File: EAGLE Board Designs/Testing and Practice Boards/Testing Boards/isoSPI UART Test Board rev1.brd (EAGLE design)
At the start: 160 x 100 mm, 51 parts, among them J1 CONNECTOR-6_μF_T_V_BLACK, J2 CONNECTOR-2_MF_T_V_, J4 CONNECTOR-2_MF_T_V_, J5 CONNECTOR-6_μF_T_V_BLACK, T1 78613/3C, T2 78613/3C, U1 MCP3204, U2 ADM4854ARZ, U3 LTC6820, U4 OPAMP_1_CHANNEL_OPA991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

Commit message: brd rev1 ready for review
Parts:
- added U$1, U$2, U$3, U$4: (no value), HyTechManufacturing:MOUNTING_M3
- added U$5: (no value), HyTechManufacturing:LOGO_HYTECH_MEDIUM
- added U$6: (no value), HyTechManufacturing:LOGO_GT_MEDIUM
- moved R20 24.5 mm to (48.5, 47.8), turned to 180 degrees
- moved R19 21.2 mm to (49.8, 49.5), turned to 180 degrees
- moved C1 17.7 mm to (57.4, 48.8)
- moved C2 17.7 mm to (57.4, 47.2)
- moved R18 17.5 mm to (49.5, 43.9), turned to 270 degrees
- moved U3 15.5 mm to (53.6, 46.7), turned to 0 degrees
- moved TP1 14.4 mm to (88.4, 20.8)
- moved R26 13.3 mm to (51.8, 41.4), turned to 270 degrees
- moved C3 12.6 mm to (32.0, 11.9), turned to 180 degrees
- moved R25 11.2 mm to (36.8, 45.7)
- moved R24 10.9 mm to (36.6, 31.5)
- moved C4 10.2 mm to (32.0, 13.7), turned to 180 degrees
- moved J2 8.89 mm to (13.0, 45.7)
- moved J4 8.89 mm to (13.0, 31.5)
- moved T2 8.89 mm to (26.2, 45.7)
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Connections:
- net IP_1 renamed DIFF_1_P
- net IP_2 renamed DIFF_2_P
- net TX+ renamed TX_P
- net TX- renamed TX_N
- removed net IM_1: R24.1, T1.2, U3.10
- removed net IM_2: R25.1, T2.2, U7.10
- removed net RX+: C7.2, D2.1, J5.2, U2.8
- removed net RX-: D2.2, J5.3, R7.1, U2.7
- new net DIFF_1_N: R24.1, T1.3, U3.10
- new net DIFF_2_N: R25.1, T2.3, U7.10
- new net RX_N: D2.1, J5.3, R7.1, U2.7
- new net RX_P: C7.2, D2.2, J5.2, U2.8
- net N$18: now also T1.2; no longer T1.3
- net N$19: now also T2.2; no longer T2.3
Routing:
- net +3V3: track 42.7 -> 192.9 mm
- net DIFF_2_P: track 0.00 -> 59.5 mm
- net DIFF_2_N: track 0.00 -> 59.5 mm
- net GND: track 0.00 -> 47.6 mm, vias 0 -> 24
- net RX_P: track 0.00 -> 44.9 mm
- net RX_N: track 0.00 -> 44.1 mm
- net DIFF_1_N: track 0.00 -> 42.1 mm
- net DIFF_1_P: track 0.00 -> 41.2 mm
- net TX_N: track 0.00 -> 33.6 mm
- net TX_P: track 0.00 -> 31.7 mm
- net UART_RX: track 5.03 -> 18.3 mm
- net UART_TX: track 5.03 -> 17.8 mm
- net TEENSY_CLK: track 23.0 -> 11.5 mm
- net TEENSY_CS: track 7.08 -> 18.0 mm
- net ADC_SDO: track 0.00 -> 10.8 mm
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- added copper zone on layer 16, net GND
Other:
- board size 160 x 100 mm -> 101.6 x 61 mm
- board text added: "HyTech Racing 2024 isoSPI UART Test Board rev1 Designed by Eric Galluzzi"

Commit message: woo
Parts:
- moved R6 0.80 mm to (78.5, 20.6)
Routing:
- net N$8: track 3.50 -> 2.63 mm
- net +3V3: track 192.9 -> 192.1 mm
- net N$9: track 3.29 -> 2.63 mm
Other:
- outline, holes or cut-outs redrawn
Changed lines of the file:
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@@
 <board>
 <plain>
-<wire x1="0" y1="58.42" x2="0" y2="2.54" width="0" layer="20"/>
+<wire x1="99.06" y1="60.96" x2="5" y2="60.96" width="0" layer="20"/>
+<wire x1="5" y1="60.96" x2="0" y2="55.96" width="0" layer="20" curve="90"/>
+<wire x1="0" y1="55.96" x2="0" y2="2.54" width="0" layer="20"/>
 <wire x1="0" y1="2.54" x2="2.54" y2="0" width="0" layer="20" curve="90"/>
 <wire x1="2.54" y1="0" x2="99.06" y2="0" width="0" layer="20"/>
@@
 <wire x1="101.6" y1="2.54" x2="101.6" y2="58.42" width="0" layer="20"/>
 <wire x1="101.6" y1="58.42" x2="99.06" y2="60.96" width="0" layer="20" curve="90"/>
-<wire x1="99.06" y1="60.96" x2="2.54" y2="60.96" width="0" layer="20"/>
-<wire x1="2.54" y1="60.96" x2="0" y2="58.42" width="0" layer="20" curve="90"/>
 <text x="46.228" y="55.88" size="0.8128" layer="25" font="vector">HyTech Racing 2024
 isoSPI UART Test Board rev1
@@
 <attribute name="VOLTAGE_MAX" value="75V" x="30.48" y="96.266" size="1.778" layer="27" rot="R180" display="off"/>
 </element>
-<element name="R6" library="HyTechDevices" package="0603-RES" value="RESISTOR_0603_2.74K" x="77.724" y="20.828" smashed="yes" rot="R270">
-<attribute name="DKPN" value="P20020CT-ND" x="7.874" y="-36.322" size="1.778" layer="27" rot="R270" display="off"/>
-<attribute name="MANUFACTURER" value="Panasonic Electronic Components" x="7.874" y="-36.322" size="1.778" layer="27" rot="R270" display="off"/>
-<attribute name="MOPN" value="667-ERJ-PB3B2741V" x="7.874" y="-36.322" size="1.778" layer="27" rot="R270" display="off"/>
-<attribute name="MPN" value="ERJ-PB3B2741V" x="7.874" y="-36.322" size="1.778" layer="27" rot="R270" display="off"/>
-<attribute name="NAME" x="76.073" y="20.828" size="0.8128" layer="25" font="vector" rot="R270" align="bottom-center"/>
-<attribute name="POWER" value="0.2W" x="7.874" y="-36.322" size="1.778" layer="27" rot="R270" display="off"/>
-<attribute name="RESISTANCE" value="2.74k" x="7.874" y="-36.322" size="1.778" layer="27" rot="R270" display="off"/>
-<attribute name="TOLERANCE" value="0.1%" x="7.874" y="-36.322" size="1.778" layer="27" rot="R270" display="off"/>
-<attribute name="VOLTAGE_CONTINUOUS" value="23.41V" x="7.874" y="-36.322" size="1.778" layer="27" rot="R270" display="off"/>
-<attribute name="VOLTAGE_MAX" value="150V" x="7.874" y="-36.322" size="1.778" layer="27" rot="R270" display="off"/>
+<element name="R6" library="HyTechDevices" package="0603-RES" value="RESISTOR_0603_2.74K" x="78.486" y="20.574" smashed="yes" rot="R270">
+<attribute name="DKPN" value="P20020CT-ND" x="8.636" y="-36.576" size="1.778" layer="27" rot="R270" display="off"/>
+<attribute name="MANUFACTURER" value="Panasonic Electronic Components" x="8.636" y="-36.576" size="1.778" layer="27" rot="R270" display="off"/>
+<attribute name="MOPN" value="667-ERJ-PB3B2741V" x="8.636" y="-36.576" size="1.778" layer="27" rot="R270" display="off"/>
+<attribute name="MPN" value="ERJ-PB3B2741V" x="8.636" y="-36.576" size="1.778" layer="27" rot="R270" display="off"/>
+<attribute name="NAME" x="76.835" y="20.574" size="0.8128" layer="25" font="vector" rot="R270" align="bottom-center"/>
+<attribute name="POWER" value="0.2W" x="8.636" y="-36.576" size="1.778" layer="27" rot="R270" display="off"/>
+<attribute name="RESISTANCE" value="2.74k" x="8.636" y="-36.576" size="1.778" layer="27" rot="R270" display="off"/>
+<attribute name="TOLERANCE" value="0.1%" x="8.636" y="-36.576" size="1.778" layer="27" rot="R270" display="off"/>
+<attribute name="VOLTAGE_CONTINUOUS" value="23.41V" x="8.636" y="-36.576" size="1.778" layer="27" rot="R270" display="off"/>
+<attribute name="VOLTAGE_MAX" value="150V" x="8.636" y="-36.576" size="1.778" layer="27" rot="R270" display="off"/>
 </element>
 <element name="R7" library="HyTechDevices" package="0603-RES" value="RESISTOR_0603_DNP" x="28.194" y="19.304" smashed="yes" rot="R90">
@@
 <attribute name="MOPN" value="595-INA823DT" x="131.826" y="-36.576" size="1.778" layer="27" display="off"/>
 <attribute name="MPN" value="INA823DT" x="131.826" y="-36.576" size="1.778" layer="27" display="off"/>
-<attribute name="NAME" x="79.375" y="21.59" size="0.8128" layer="25" font="vector" rot="R90" align="bottom-center"/>
+<attribute name="NAME" x="85.979" y="20.32" size="0.8128" layer="25" font="vector" rot="R90" align="bottom-center"/>
 </element>
 <element name="U7" library="HyTechDevices" package="MSOP-16" value="LTC6820" x="83.82" y="43.688" smashed="yes" rot="R90">
@@
 <wire x1="59.194" y1="51.308" x2="56.654" y2="48.768" width="0.254" layer="1"/>
 <wire x1="51.474" y1="40.552" x2="50.292" y2="39.37" width="0.254" layer="1"/>
-<wire x1="50.292" y1="39.37" x2="49.276" y2="38.354" width="0.254" layer="1"/>
 <wire x1="51.474" y1="40.552" x2="51.816" y2="40.552" width="0.254" layer="1"/>
 <wire x1="49.53" y1="40.132" x2="50.292" y2="39.37" width="0.254" layer="1"/>
 <wire x1="49.53" y1="40.132" x2="49.53" y2="43.092" width="0.254" layer="1"/>
-<wire x1="49.276" y1="23.622" x2="52.832" y2="20.066" width="0.254" layer="1"/>
-<wire x1="49.276" y1="38.354" x2="49.276" y2="23.622" width="0.254" layer="1"/>
+<wire x1="50.292" y1="22.606" x2="52.832" y2="20.066" width="0.254" layer="1"/>
+<wire x1="50.292" y1="39.37" x2="50.292" y2="22.606" width="0.254" layer="1"/>
 <wire x1="70.358" y1="28.956" x2="65.786" y2="28.956" width="0.254" layer="1"/>
 <wire x1="65.786" y1="28.956" x2="64.008" y2="27.178" width="0.254" layer="1"/>
@@
 <wire x1="36.957" y1="21.717" x2="36.957" y2="20.6375" width="0.254" layer="1"/>
 <wire x1="36.576" y1="22.098" x2="36.957" y2="21.717" width="0.254" layer="1"/>
-<wire x1="24.9776625" y1="15.1384" x2="27.8384" y2="15.1384" width="0.254" layer="1"/>
+<wire x1="24.9776625" y1="15.1384" x2="25.908" y2="15.1384" width="0.254" layer="1"/>
+<wire x1="25.908" y1="15.1384" x2="27.8384" y2="15.1384" width="0.254" layer="1"/>
 <wire x1="27.8384" y1="15.1384" x2="29.8704" y2="17.1704" width="0.254" layer="1"/>
 <wire x1="29.8704" y1="17.1704" x2="35.2044" y2="17.1704" width="0.254" layer="1"/>
@@
 <wire x1="87.718" y1="30.48" x2="89.408" y2="28.79" width="0.254" layer="1"/>
 <wire x1="89.408" y1="28.79" x2="89.408" y2="28.182" width="0.254" layer="1"/>
-<wire x1="84.216" y1="30.564" x2="85.402" y2="31.75" width="0.254" layer="1"/>
-<wire x1="86.448" y1="31.75" x2="87.718" y2="30.48" width="0.254" layer="1"/>
-<wire x1="85.402" y1="31.75" x2="86.448" y2="31.75" width="0.254" layer="1"/>
+<wire x1="84.216" y1="30.564" x2="85.148" y2="31.496" width="0.254" layer="1"/>
+<wire x1="86.702" y1="31.496" x2="87.718" y2="30.48" width="0.254" layer="1"/>
+<wire x1="85.148" y1="31.496" x2="86.702" y2="31.496" width="0.254" layer="1"/>
 <wire x1="84.216" y1="30.564" x2="83.284" y2="31.496" width="0.254" layer="1"/>
 <wire x1="83.284" y1="31.496" x2="81.788" y2="31.496" width="0.254" layer="1"/>
@@
 <contactref element="U5" pad="1"/>
 <contactref element="R6" pad="2"/>
-<wire x1="77.724" y1="19.978" x2="79.7315" y2="17.9705" width="0.254" layer="1"/>
-<wire x1="79.7315" y1="17.9705" x2="80.391" y2="17.9705" width="0.254" layer="1"/>
+<wire x1="78.486" y1="19.724" x2="80.2395" y2="17.9705" width="0.254" layer="1"/>
+<wire x1="80.2395" y1="17.9705" x2="80.391" y2="17.9705" width="0.254" layer="1"/>
 </signal>
 <signal name="N$9" airwireshidden="yes">
 <contactref element="R6" pad="1"/>
 <contactref element="U5" pad="8"/>
-<wire x1="77.724" y1="21.678" x2="79.2235" y2="23.1775" width="0.254" layer="1"/>
-<wire x1="79.2235" y1="23.1775" x2="80.391" y2="23.1775" width="0.254" layer="1"/>
+<wire x1="78.486" y1="21.424" x2="80.2395" y2="23.1775" width="0.254" layer="1"/>
+<wire x1="80.2395" y1="23.1775" x2="80.391" y2="23.1775" width="0.254" layer="1"/>
 </signal>
 <signal name="CH_1-" airwireshidden="yes">

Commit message: board review
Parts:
- moved J1 1.78 mm to (84.8, 8.64), flipped to the top, turned to 270 degrees
- moved U$5 1.02 mm to (10.2, 53.3)
- moved C20 0.76 mm to (34.0, 46.5)
- moved J2 0.76 mm to (13.0, 46.5)
- moved R25 0.76 mm to (36.8, 46.5)
- moved T2 0.76 mm to (26.2, 46.5)
- moved D2 0.36 mm to (20.8, 19.6)
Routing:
- net CH3: track 39.5 -> 48.4 mm
- net CH2: track 33.8 -> 39.8 mm
- net TX_P: track 31.7 -> 37.6 mm
- net TX_N: track 33.6 -> 39.5 mm
- net CH_1+: track 5.35 -> 10.1 mm
- net 5VIN: track 12.5 -> 9.67 mm
- net DIFF_1_N: track 42.1 -> 39.3 mm
- net CH_1-: track 4.63 -> 6.41 mm
- net DIFF_2_N: track 59.5 -> 57.9 mm
- net +3V3: track 192.1 -> 193.4 mm
- net DIFF_2_P: track 59.5 -> 58.2 mm
- net DIFF_1_P: track 41.2 -> 40.1 mm
- net UART_RX: track 18.3 -> 19.0 mm
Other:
- outline, holes or cut-outs redrawn

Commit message: awesome
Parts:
- added R2: RESISTOR_1206_HV46.4K, HyTechDevices:1206-RES
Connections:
- net +3V3: now also R2.1
- net GND: now also R2.2
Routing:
- net +3V3: track 193.4 -> 201.1 mm
- net N$7: track 0.00 -> 1.88 mm, vias 0 -> 1

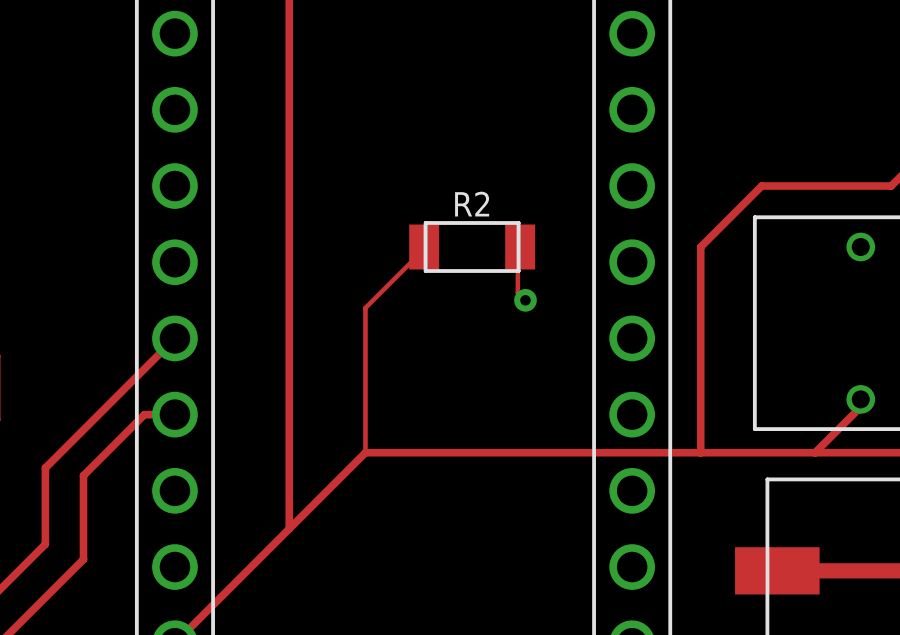
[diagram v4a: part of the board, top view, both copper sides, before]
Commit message: There was a resistor added!
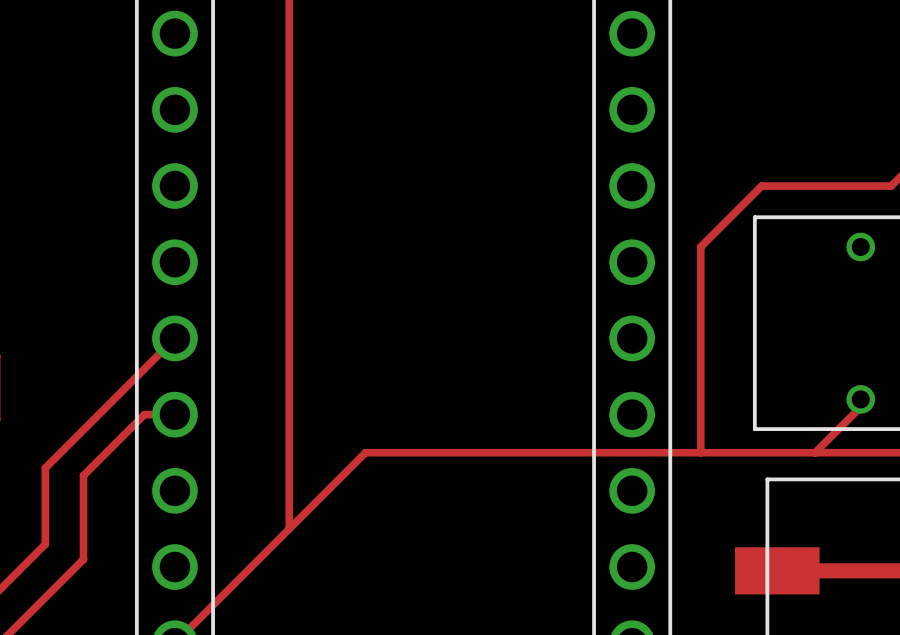
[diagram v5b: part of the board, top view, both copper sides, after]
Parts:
- removed R2: RESISTOR_1206_HV46.4K, HyTechDevices:1206-RES
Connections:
- net +3V3: no longer R2.1
- net GND: no longer R2.2
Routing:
- net +3V3: track 201.1 -> 193.4 mm
- net N$7: track 1.88 -> 0.00 mm, vias 1 -> 0
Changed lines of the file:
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@@
 <attribute name="NAME" x="19.05" y="18.542" size="0.635" layer="25" font="vector" rot="R270" align="top-center"/>
-</element>
-<element name="R2" library="HyTechDevices" package="1206-RES" value="RESISTOR_1206_HV46.4K" x="56.388" y="26.924" smashed="yes">
-<attribute name="DKPN" value="RHM46.4KAICT-ND" x="56.388" y="26.924" size="1.778" layer="27" display="off"/>
-<attribute name="MANUFACTURER" value="Rohm Semiconductor" x="56.388" y="26.924" size="1.778" layer="27" display="off"/>
-<attribute name="MOPN" value="755-KTR18EZPF4642" x="56.388" y="26.924" size="1.778" layer="27" display="off"/>
-<attribute name="MPN" value="KTR18EZPF4642" x="56.388" y="26.924" size="1.778" layer="27" display="off"/>
-<attribute name="NAME" x="56.388" y="27.94" size="0.8128" layer="25" font="vector" align="bottom-center"/>
-<attribute name="POWER" value="0.25W" x="56.388" y="26.924" size="1.778" layer="27" display="off"/>
-<attribute name="RESISTANCE" value="46.4k" x="56.388" y="26.924" size="1.778" layer="27" display="off"/>
-<attribute name="TOLERANCE" value="1%" x="56.388" y="26.924" size="1.778" layer="27" display="off"/>
-<attribute name="VOLTAGE_CONTINUOUS" value="107.7V" x="56.388" y="26.924" size="1.778" layer="27" display="off"/>
-<attribute name="VOLTAGE_MAX" value="500V" x="56.388" y="26.924" size="1.778" layer="27" display="off"/>
 </element>
 </elements>
@@
 <wire x1="19.8247" y1="19.558" x2="18.542" y2="19.558" width="0.254" layer="1"/>
 <via x="18.542" y="19.558" extent="1-16" drill="0.3556"/>
-<contactref element="R2" pad="2"/>
 <wire x1="85.9255" y1="44.938" x2="88.888" y2="44.958" width="0" layer="19" extent="1-1"/>
 <wire x1="85.9255" y1="41.938" x2="85.9255" y2="44.938" width="0" layer="19" extent="1-1"/>
@@
 <wire x1="16.002" y1="17.7292" x2="18.542" y2="19.558" width="0" layer="19" extent="1-1"/>
 <wire x1="61.722" y1="8.636" x2="46.482" y2="11.176" width="0" layer="19" extent="1-1"/>
-<wire x1="57.988" y1="26.924" x2="16.002" y2="17.7292" width="0" layer="19" extent="1-1"/>
 </signal>
 <signal name="+3V3" airwireshidden="yes">
@@
 <wire x1="50.292" y1="17.526" x2="52.832" y2="20.066" width="0.254" layer="1"/>
 <wire x1="52.832" y1="20.066" x2="64.008" y2="20.066" width="0.254" layer="1"/>
-<contactref element="R2" pad="1"/>
-<wire x1="54.864" y1="26.924" x2="52.832" y2="24.892" width="0.1524" layer="1"/>
-<wire x1="52.832" y1="24.892" x2="52.832" y2="20.066" width="0.1524" layer="1"/>
-<wire x1="54.864" y1="26.924" x2="54.788" y2="26.924" width="0" layer="19" extent="1-1"/>
 </signal>
 <signal name="TEENSY_CLK" airwireshidden="yes">
@@
 <wire x1="79.502" y1="32.004" x2="79.502" y2="34.2265" width="0.254" layer="1"/>
 </signal>
-<signal name="N$7">
-<via x="58.166" y="25.146" extent="1-16" drill="0.35"/>
-<wire x1="57.912" y1="26.924" x2="57.912" y2="25.4" width="0.1524" layer="1"/>
-<wire x1="57.912" y1="25.4" x2="58.166" y2="25.146" width="0.1524" layer="1"/>
-</signal>
 </signals>
